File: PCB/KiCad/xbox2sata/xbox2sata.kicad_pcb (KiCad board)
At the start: 4 copper layers, 156 x 90 mm, 7 parts, among them J1 61203921621, J2 67800-8025, J3 90151-2140, U1 88SA8052, Y1 ABLS-25.000MHZ-B4-F-T

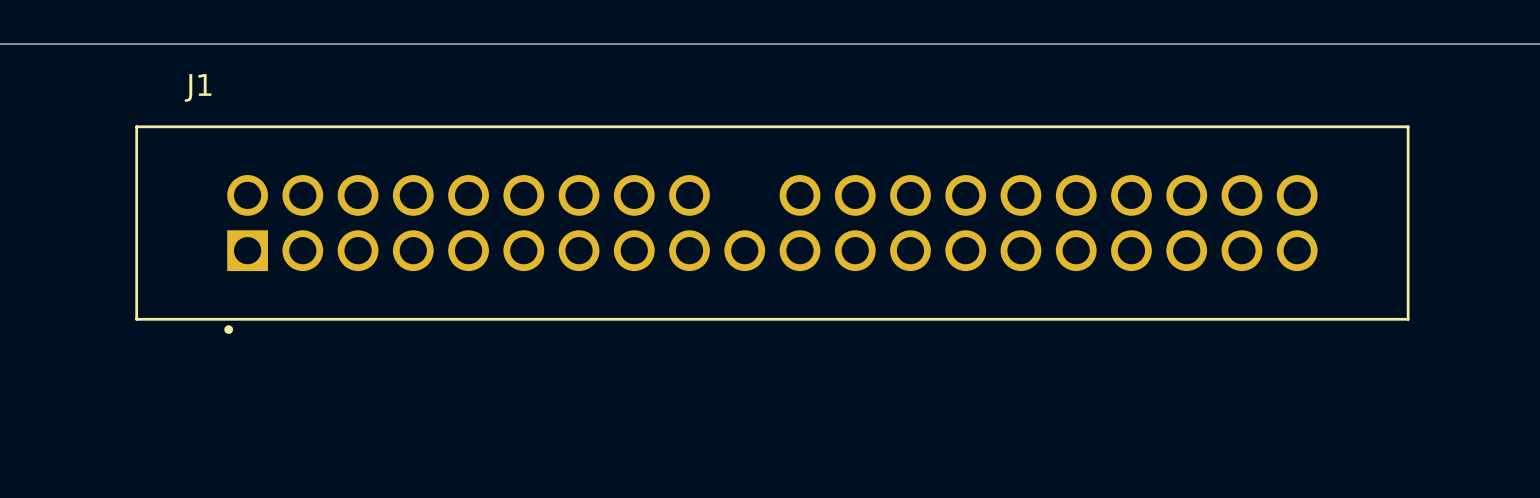
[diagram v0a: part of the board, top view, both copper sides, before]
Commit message: PCB folder structure
Created two sub folders in PCB; Proteus and KiCad and moved respective files into folders.
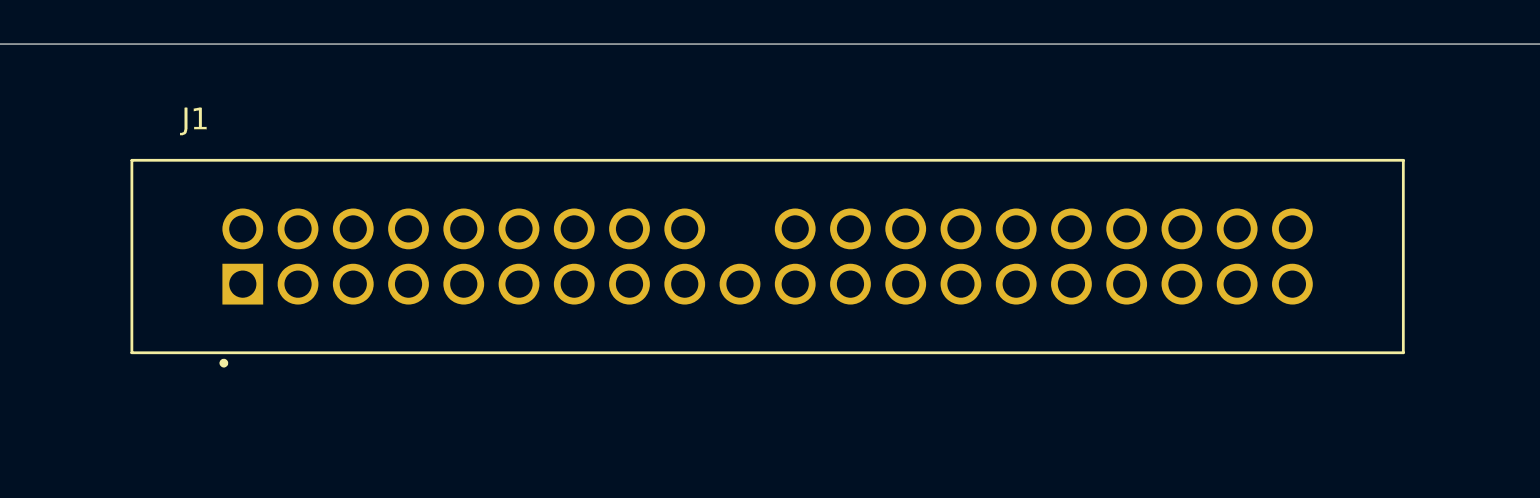
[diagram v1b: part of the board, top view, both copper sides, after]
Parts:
- moved J1 1.56 mm to (167.7, 73.3)
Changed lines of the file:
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@@
 			(pintype "power_in")
 		)
-		(model "${KICAD8_3DMODEL_DIR}/Package_DFN_QFN.3dshapes/QFN-64-1EP_9x9mm_P0.5mm_EP3.4x3.4mm.wrl"
+		(model "${KICAD8_3DMODEL_DIR}/Package_DFN_QFN.3dshapes/QFN-64-1EP_9x9mm_P0.5mm_EP7.35x7.35mm.step"
 			(offset
 				(xyz 0 0 0)
@@
 			(pintype "passive")
 		)
-		(model "D:/Gaming hardware/Microsoft XBox/Modifications/HDD/XBox-IDE to-SATA/PCB/Imports/LIB_ABLS-25.000MHZ-B4-F-T KiCad/ABLS-25.000MHZ-B4-F-T.stp"
+		(model "D:/Gaming hardware/Microsoft XBox/Modifications/HDD/XBox-IDE to-SATA/PCB/KiCad/Imports/LIB_ABLS-25.000MHZ-B4-F-T KiCad/ABLS-25.000MHZ-B4-F-T.stp"
 			(offset
 				(xyz 0 0 2.7)
@@
 	(footprint "xbox2sata:WURTH-ELEKTRONIK_61203921621"
 		(layer "F.Cu")
-		(at 167.87 71.73)
+		(at 167.65 73.27)
 		(descr "IDE socket")
 		(tags "IDE socket")
@@
 			)
 		)
-		(property "Description" "IDE Socket"
+		(property "Description" "IDE male header"
 			(at 8.5 6 0)
 			(unlocked yes)
@@
 			)
 		)
+		(sheetname "Root")
+		(sheetfile "xbox2sata.kicad_sch")
 		(attr through_hole)
 		(fp_line
@@
 			(solder_mask_margin 0.102)
 		)
-		(model "D:/Gaming hardware/Microsoft XBox/Modifications/HDD/XBox-IDE to-SATA/PCB/Imports/1761633-2.stp"
+		(model "D:/Gaming hardware/Microsoft XBox/Modifications/HDD/XBox-IDE to-SATA/PCB/KiCad/Imports/61203921621_Download_STP_61203921621_rev1.stp"
 			(offset
-				(xyz 0 0 9.5)
+				(xyz 0 0 5)
 			)
 			(scale
@@
 			(pintype "power_in")
 		)
-		(model "D:/Gaming hardware/Microsoft XBox/Modifications/HDD/XBox-IDE to-SATA/PCB/Imports/678008025.stp"
+		(model "D:/Gaming hardware/Microsoft XBox/Modifications/HDD/XBox-IDE to-SATA/PCB/KiCad/Imports/678008025.stp"
 			(offset
 				(xyz -4 0.8 4)
@@
 			(pintype "passive")
 		)
-		(model "D:/Gaming hardware/Microsoft XBox/Modifications/HDD/XBox-IDE to-SATA/PCB/Imports/Molex 90151-2140 KiCad/90151-2140.stp"
+		(model "D:/Gaming hardware/Microsoft XBox/Modifications/HDD/XBox-IDE to-SATA/PCB/KiCad/Imports/Molex 90151-2140 KiCad/90151-2140.stp"
 			(offset
 				(xyz 24.1 1.3 4)

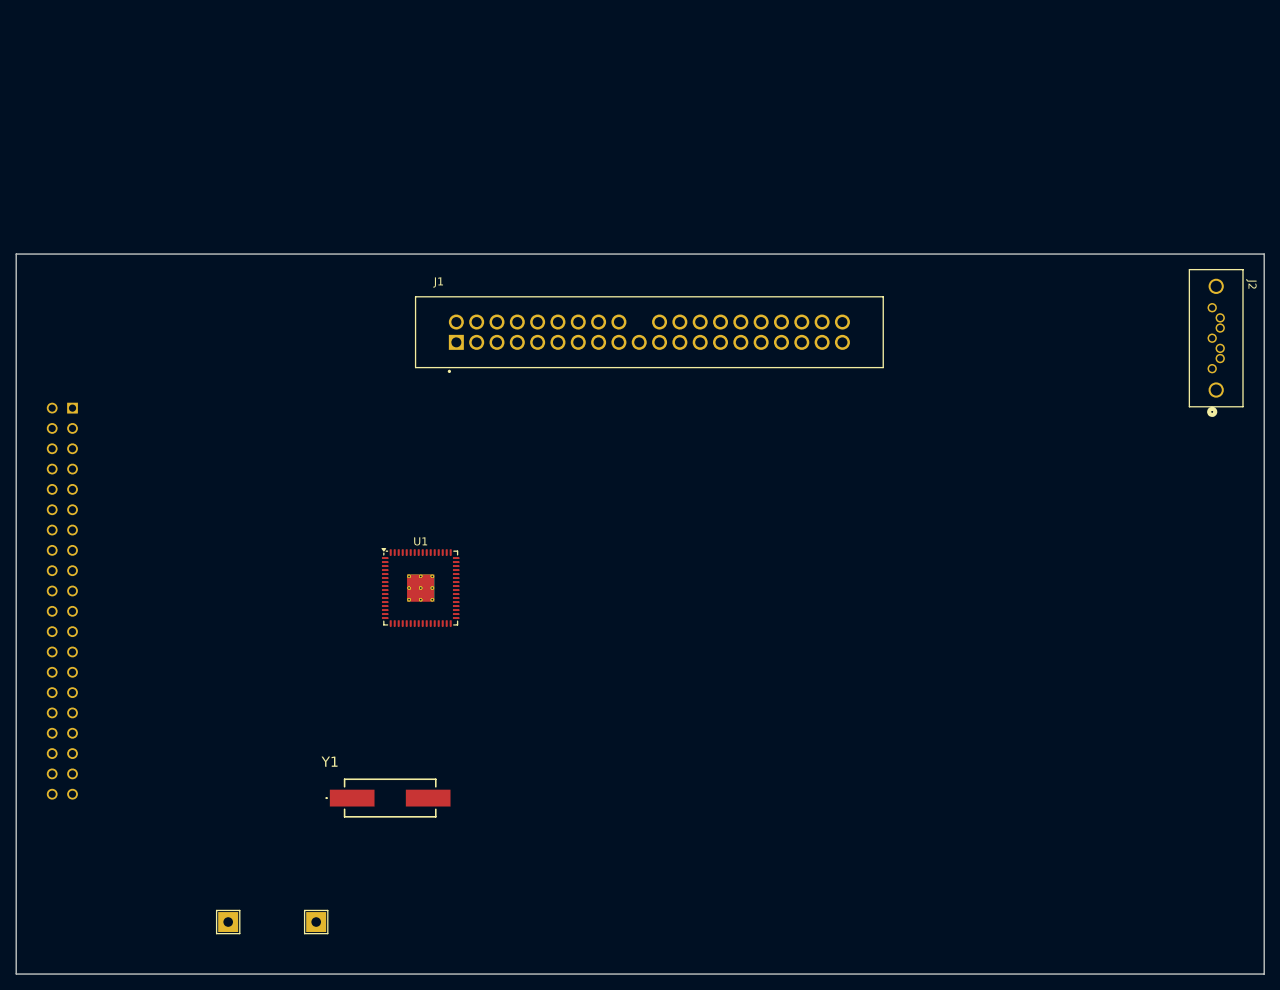
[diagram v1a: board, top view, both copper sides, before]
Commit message: KiCad updates
Nets and some components added
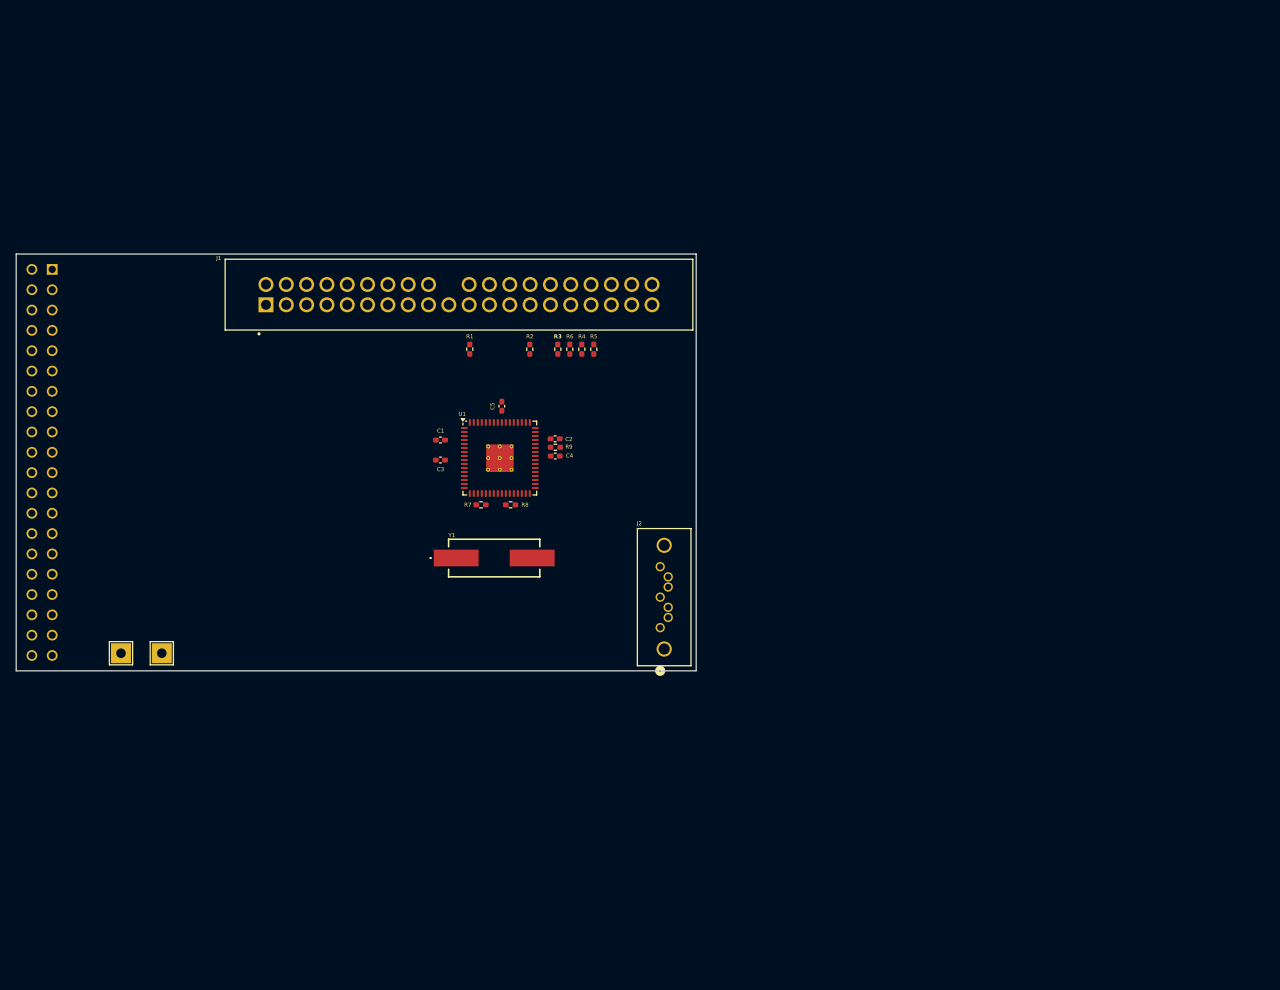
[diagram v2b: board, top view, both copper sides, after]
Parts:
- added C1: 100nF, Capacitor_SMD:C_0402_1005Metric_Pad0.74x0.62mm_HandSolder, F.Cu at (141.5, 86.8)
- added C2: 100nF, Capacitor_SMD:C_0402_1005Metric_Pad0.74x0.62mm_HandSolder, F.Cu at (155.9, 86.6)
- added C3: 100nF, Capacitor_SMD:C_0402_1005Metric_Pad0.74x0.62mm_HandSolder, F.Cu at (141.5, 89.2)
- added C4: 100nF, Capacitor_SMD:C_0402_1005Metric_Pad0.74x0.62mm_HandSolder, F.Cu at (155.9, 88.8)
- added C5: 100nF, Capacitor_SMD:C_0402_1005Metric_Pad0.74x0.62mm_HandSolder, F.Cu at (149.2, 82.5)
- added R1: 5.6K, Resistor_SMD:R_0402_1005Metric_Pad0.72x0.64mm_HandSolder, F.Cu at (145.2, 75.4)
- added R2: 4.7K, Resistor_SMD:R_0402_1005Metric_Pad0.72x0.64mm_HandSolder, F.Cu at (152.7, 75.4)
- added R3: 10K, Resistor_SMD:R_0402_1005Metric_Pad0.72x0.64mm_HandSolder, F.Cu at (156.2, 75.4)
- added R4: 10K, Resistor_SMD:R_0402_1005Metric_Pad0.72x0.64mm_HandSolder, F.Cu at (159.2, 75.4)
- added R5: 10K, Resistor_SMD:R_0402_1005Metric_Pad0.72x0.64mm_HandSolder, F.Cu at (160.7, 75.4)
- added R6: 10K, Resistor_SMD:R_0402_1005Metric_Pad0.72x0.64mm_HandSolder, F.Cu at (157.7, 75.4)
- added R7: 10K, Resistor_SMD:R_0402_1005Metric_Pad0.72x0.64mm_HandSolder, F.Cu at (146.6, 94.8)
- added R8: 10K, Resistor_SMD:R_0402_1005Metric_Pad0.72x0.64mm_HandSolder, F.Cu at (150.3, 94.8)
- added R9: 10K, Resistor_SMD:R_0402_1005Metric_Pad0.72x0.64mm_HandSolder, F.Cu at (155.9, 87.7)
- moved J2 76.2 mm to (169.0, 110.2)
- moved TP1 41.5 mm to (101.6, 113.4)
- moved TP2 34.6 mm to (106.7, 113.4)
- moved Y1 32.7 mm to (148.2, 101.5)
- moved J1 24.3 mm to (143.8, 68.6)
- moved U1 19.0 mm to (148.9, 89.0)
- moved J3 17.5 mm to (93.0, 65.4)
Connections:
- J1 pad 1: unconnected-(J1-Pad1) -> RESET-
- J1 pad 10: unconnected-(J1-Pad10) -> DD11
- J1 pad 11: unconnected-(J1-Pad11) -> DD3
- J1 pad 12: unconnected-(J1-Pad12) -> DD12
- J1 pad 13: unconnected-(J1-Pad13) -> DD2
- J1 pad 14: unconnected-(J1-Pad14) -> DD13
- J1 pad 15: unconnected-(J1-Pad15) -> DD1
- J1 pad 16: unconnected-(J1-Pad16) -> DD14
- J1 pad 17: unconnected-(J1-Pad17) -> DD0
- J1 pad 18: unconnected-(J1-Pad18) -> DD15
- J1 pad 19: unconnected-(J1-Pad19) -> GND
- J1 pad 2: unconnected-(J1-Pad2) -> GND
- J1 pad 21: unconnected-(J1-Pad21) -> DMARQ
- J1 pad 22: unconnected-(J1-Pad22) -> GND
- J1 pad 23: unconnected-(J1-Pad23) -> DIOW-
- J1 pad 24: unconnected-(J1-Pad24) -> GND
- J1 pad 25: unconnected-(J1-Pad25) -> DIOR-
- J1 pad 26: unconnected-(J1-Pad26) -> GND
- J1 pad 27: unconnected-(J1-Pad27) -> IORDY
- J1 pad 28: unconnected-(J1-Pad28) -> CSEL
- J1 pad 29: unconnected-(J1-Pad29) -> DMACK-
- J1 pad 3: unconnected-(J1-Pad3) -> DD7
- J1 pad 30: unconnected-(J1-Pad30) -> GND
- J1 pad 31: unconnected-(J1-Pad31) -> INTRQ
- J1 pad 32: unconnected-(J1-Pad32) -> Net-(J1-Pad32)
- J1 pad 33: unconnected-(J1-Pad33) -> DA1
- J1 pad 34: unconnected-(J1-Pad34) -> PDIAG-
- J1 pad 35: unconnected-(J1-Pad35) -> DA0
- J1 pad 36: unconnected-(J1-Pad36) -> DA2
- J1 pad 37: unconnected-(J1-Pad37) -> CS0-
- J1 pad 38: unconnected-(J1-Pad38) -> CS1-
- J1 pad 39: unconnected-(J1-Pad39) -> Net-(J1-Pad39)
- J1 pad 4: unconnected-(J1-Pad4) -> DD8
- J1 pad 40: unconnected-(J1-Pad40) -> GND
- J1 pad 5: unconnected-(J1-Pad5) -> DD6
- J1 pad 6: unconnected-(J1-Pad6) -> DD9
- J1 pad 7: unconnected-(J1-Pad7) -> DD5
- J1 pad 8: unconnected-(J1-Pad8) -> DD10
- J1 pad 9: unconnected-(J1-Pad9) -> DD4
- J3 pad 1: unconnected-(J3-Pad1) -> RESET-
- J3 pad 10: unconnected-(J3-Pad10) -> DD11
- J3 pad 11: unconnected-(J3-Pad11) -> DD3
- J3 pad 12: unconnected-(J3-Pad12) -> DD12
- J3 pad 13: unconnected-(J3-Pad13) -> DD2
- J3 pad 14: unconnected-(J3-Pad14) -> DD13
- J3 pad 15: unconnected-(J3-Pad15) -> DD1
- J3 pad 16: unconnected-(J3-Pad16) -> DD14
- J3 pad 17: unconnected-(J3-Pad17) -> DD0
- J3 pad 18: unconnected-(J3-Pad18) -> DD15
- J3 pad 19: unconnected-(J3-Pad19) -> GND
- J3 pad 2: unconnected-(J3-Pad2) -> GND
- J3 pad 21: unconnected-(J3-Pad21) -> DMARQ
- J3 pad 22: unconnected-(J3-Pad22) -> GND
- J3 pad 23: unconnected-(J3-Pad23) -> DIOW-
- J3 pad 24: unconnected-(J3-Pad24) -> GND
- J3 pad 25: unconnected-(J3-Pad25) -> DIOR-
- J3 pad 26: unconnected-(J3-Pad26) -> GND
- J3 pad 27: unconnected-(J3-Pad27) -> IORDY
- J3 pad 28: unconnected-(J3-Pad28) -> CSEL
- J3 pad 29: unconnected-(J3-Pad29) -> DMACK-
- J3 pad 3: unconnected-(J3-Pad3) -> DD7
- J3 pad 30: unconnected-(J3-Pad30) -> GND
- J3 pad 31: unconnected-(J3-Pad31) -> INTRQ
- J3 pad 32: unconnected-(J3-Pad32) -> IOCS16
- J3 pad 33: unconnected-(J3-Pad33) -> DA1
- J3 pad 34: unconnected-(J3-Pad34) -> PDIAG-
- J3 pad 35: unconnected-(J3-Pad35) -> DA0
- J3 pad 36: unconnected-(J3-Pad36) -> DA2
- J3 pad 37: unconnected-(J3-Pad37) -> CS0-
- J3 pad 38: unconnected-(J3-Pad38) -> CS1-
- J3 pad 39: unconnected-(J3-Pad39) -> DASP-
- J3 pad 4: unconnected-(J3-Pad4) -> DD8
- J3 pad 40: unconnected-(J3-Pad40) -> GND
- J3 pad 5: unconnected-(J3-Pad5) -> DD6
- J3 pad 6: unconnected-(J3-Pad6) -> DD9
- J3 pad 7: unconnected-(J3-Pad7) -> DD5
- J3 pad 8: unconnected-(J3-Pad8) -> DD10
- J3 pad 9: unconnected-(J3-Pad9) -> DD4
- TP1 pad 1: unconnected-(TP1-Pad1) -> GND
- TP2 pad 1: unconnected-(TP2-Pad1) -> 3V3
- U1 pad 1: unconnected-(U1-H_DD13-Pad1) -> DD13
- U1 pad 10: unconnected-(U1-H_DD10-Pad10) -> DD10
- U1 pad 11: unconnected-(U1-H_DD5-Pad11) -> DD5
- U1 pad 12: unconnected-(U1-H_DD9-Pad12) -> DD9
- U1 pad 13: unconnected-(U1-H_DD6-Pad13) -> DD6
- U1 pad 14: unconnected-(U1-H_DD8-Pad14) -> DD8
- U1 pad 15: unconnected-(U1-H_DD7-Pad15) -> DD7
- U1 pad 16: unconnected-(U1-H_RESET_N-Pad16) -> RESET-
- U1 pad 17: unconnected-(U1-RST_N-Pad17) -> RST-
- U1 pad 18: unconnected-(U1-CNFG0-Pad18) -> CNFG0
- U1 pad 19: unconnected-(U1-CNFG1-Pad19) -> CNFG1
- U1 pad 2: unconnected-(U1-H_DD2-Pad2) -> DD2
- U1 pad 20: unconnected-(U1-CNFG2-Pad20) -> CNFG2
- U1 pad 21: unconnected-(U1-ATAIOS-Pad21) -> Net-(U1-ATAIOS)
- U1 pad 22: unconnected-(U1-XTLIN/OSC-Pad22) -> XTLIN
- U1 pad 23: unconnected-(U1-XTLOUT-Pad23) -> XTLOUT
- U1 pad 24: unconnected-(U1-VAA-Pad24) -> VAA
- U1 pad 25: unconnected-(U1-VSS-Pad25) -> VSS
- U1 pad 26: unconnected-(U1-ISET-Pad26) -> Net-(U1-ISET)
- U1 pad 27: unconnected-(U1-RX_P-Pad27) -> RX_P
- U1 pad 28: unconnected-(U1-RX_M-Pad28) -> RX_M
- U1 pad 29: unconnected-(U1-VAA-Pad29) -> VAA
- U1 pad 3: unconnected-(U1-H_DD12-Pad3) -> DD12
- U1 pad 30: unconnected-(U1-VSS-Pad30) -> VSS
- U1 pad 31: unconnected-(U1-TX_M-Pad31) -> TX_M
- U1 pad 32: unconnected-(U1-TX_P-Pad32) -> TX_P
- U1 pad 33: unconnected-(U1-T0-Pad33) -> T0
- U1 pad 34: unconnected-(U1-T1-Pad34) -> PDIAG
- U1 pad 35: unconnected-(U1-T2-Pad35) -> T1
- U1 pad 36: unconnected-(U1-T3-Pad36) -> T3
- U1 pad 37: unconnected-(U1-T4-Pad37) -> T4
- U1 pad 38: unconnected-(U1-T5-Pad38) -> T5
- U1 pad 39: unconnected-(U1-T6-Pad39) -> T6
- U1 pad 4: unconnected-(U1-VDDIO-Pad4) -> 3V3
- U1 pad 40: unconnected-(U1-T7-Pad40) -> T7
- U1 pad 41: unconnected-(U1-VDD-Pad41) -> 1V2
- U1 pad 42: unconnected-(U1-GND-Pad42) -> GND
- U1 pad 43: unconnected-(U1-UAI-Pad43) -> Net-(U1-UAI)
- U1 pad 44: unconnected-(U1-VDDIO-Pad44) -> 3V3
- U1 pad 45: unconnected-(U1-UAO-Pad45) -> LED-
- U1 pad 46: unconnected-(U1-H_PDIAG_N-Pad46) -> PDIAG-
- U1 pad 47: unconnected-(U1-H_CS_N1-Pad47) -> CS1-
- U1 pad 48: unconnected-(U1-H_CS_N0-Pad48) -> CS0-
- U1 pad 49: unconnected-(U1-H_DA2-Pad49) -> DA2
- U1 pad 5: unconnected-(U1-H_DD3-Pad5) -> DD3
- U1 pad 50: unconnected-(U1-H_DA0-Pad50) -> DA0
- U1 pad 51: unconnected-(U1-H_DA1-Pad51) -> DA1
- U1 pad 52: unconnected-(U1-T8-Pad52) -> T8
- U1 pad 53: unconnected-(U1-H_INTRQ-Pad53) -> INTRQ
- U1 pad 54: unconnected-(U1-H_DMACK_N-Pad54) -> DMACK-
- U1 pad 55: unconnected-(U1-H_IORDY-Pad55) -> IORDY
- U1 pad 56: unconnected-(U1-VDD-Pad56) -> 1V2
- U1 pad 57: unconnected-(U1-GND-Pad57) -> GND
- U1 pad 58: unconnected-(U1-H_DIOR_N-Pad58) -> DIOR-
- U1 pad 59: unconnected-(U1-H_DIOW_N-Pad59) -> DIOW-
- U1 pad 6: unconnected-(U1-H_DD11-Pad6) -> DD11
- U1 pad 60: unconnected-(U1-H_DMARQ-Pad60) -> DMARQ
- U1 pad 61: unconnected-(U1-H_DD15-Pad61) -> DD15
- U1 pad 62: unconnected-(U1-H_DD0-Pad62) -> DD0
- U1 pad 63: unconnected-(U1-H_DD14-Pad63) -> DD14
- U1 pad 64: unconnected-(U1-H_DD1-Pad64) -> DD1
- U1 pad 7: unconnected-(U1-H_DD4-Pad7) -> DD4
- U1 pad 8: unconnected-(U1-GND-Pad8) -> GND
- U1 pad 9: unconnected-(U1-VDD-Pad9) -> 1V2
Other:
- board size 156 x 90 mm -> 85 x 52.1 mm

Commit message: KiCad update
Added to schematic and pcb
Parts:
- added C10: 10nF, Resistor_SMD:R_0402_1005Metric_Pad0.72x0.64mm_HandSolder, F.Cu at (123.4, 74.5)
- added C11: 10nF, Resistor_SMD:R_0402_1005Metric_Pad0.72x0.64mm_HandSolder, F.Cu at (123.4, 73.3)
- added C12: 10nF, Resistor_SMD:R_0402_1005Metric_Pad0.72x0.64mm_HandSolder, F.Cu at (123.2, 66.6)
- added C13: 10nF, Resistor_SMD:R_0402_1005Metric_Pad0.72x0.64mm_HandSolder, F.Cu at (123.3, 65.1)
- added C14: 10nF, Capacitor_SMD:C_0402_1005Metric_Pad0.74x0.62mm_HandSolder, F.Cu at (118.9, 111.4)
- added C15: 100nF, Capacitor_SMD:C_0402_1005Metric_Pad0.74x0.62mm_HandSolder, F.Cu at (118.9, 108.9)
- added C16: 100nF, Capacitor_SMD:C_0402_1005Metric_Pad0.74x0.62mm_HandSolder, F.Cu at (118.9, 107.7)
- added C17: 10nF, Capacitor_SMD:C_0402_1005Metric_Pad0.74x0.62mm_HandSolder, F.Cu at (118.9, 106.4)
- added C6: 1uF, Capacitor_SMD:C_0603_1608Metric_Pad1.08x0.95mm_HandSolder, F.Cu at (113.9, 103.2)
- added C7: 1uF, Capacitor_SMD:C_0603_1608Metric_Pad1.08x0.95mm_HandSolder, F.Cu at (114.4, 113.7)
- added C8: 18pF, Capacitor_SMD:C_0402_1005Metric_Pad0.74x0.62mm_HandSolder, F.Cu at (108.9, 81.1)
- added C9: 18pF, Capacitor_SMD:C_0402_1005Metric_Pad0.74x0.62mm_HandSolder, F.Cu at (118.5, 81.1)
- added IC1: TLV1117LV12DCYR, xbox2sata:SOT230P700X180-4N, F.Cu at (113.0, 108.4)
- added L1: L, Inductor_SMD:L_0402_1005Metric_Pad0.77x0.64mm_HandSolder, F.Cu at (118.9, 110.2)
- added R10: 1M, Resistor_SMD:R_0402_1005Metric_Pad0.72x0.64mm_HandSolder, F.Cu at (113.2, 90.0)
- added R11: 100, Resistor_SMD:R_0402_1005Metric_Pad0.72x0.64mm_HandSolder, F.Cu at (107.7, 69.9)
- added R12: 10K, Resistor_SMD:R_0402_1005Metric_Pad0.72x0.64mm_HandSolder, F.Cu at (107.8, 63.5)
- added R13: 10K, Resistor_SMD:R_0402_1005Metric_Pad0.72x0.64mm_HandSolder, F.Cu at (107.6, 65.0)
- added R14: 10K, Resistor_SMD:R_0402_1005Metric_Pad0.72x0.64mm_HandSolder, F.Cu at (107.7, 66.8)
- added R15: 4.7K, Resistor_SMD:R_0402_1005Metric_Pad0.72x0.64mm_HandSolder, F.Cu at (110.4, 76.3)
- added R16: 10K, Resistor_SMD:R_0402_1005Metric_Pad0.72x0.64mm_HandSolder, F.Cu at (112.5, 76.4)
- added R17: 10K, Resistor_SMD:R_0402_1005Metric_Pad0.72x0.64mm_HandSolder, F.Cu at (113.7, 76.4)
- added R18: 10K, Resistor_SMD:R_0402_1005Metric_Pad0.72x0.64mm_HandSolder, F.Cu at (121.1, 71.7)
- moved R5 62.6 mm to (106.3, 106.4), turned to 180 degrees
- moved R4 60.6 mm to (106.3, 104.9), turned to 0 degrees
- moved R6 58.6 mm to (106.3, 103.4), turned to 180 degrees
- moved R3 56.5 mm to (106.3, 101.9), turned to 0 degrees
- moved J2 54.3 mm to (128.2, 74.4)
- moved R2 51.8 mm to (106.3, 98.4), turned to 0 degrees
- moved J1 49.0 mm to (99.6, 89.6), turned to -90 degrees
- moved R8 48.5 mm to (107.7, 71.6), turned to 0 degrees
- moved R7 47.0 mm to (107.8, 68.3)
- moved C4 42.8 mm to (114.9, 76.4), turned to -90 degrees
- moved R1 41.9 mm to (106.3, 90.9), turned to 0 degrees
- moved R9 41.5 mm to (116.0, 76.4), turned to -90 degrees
- moved C2 40.2 mm to (117.0, 76.4), turned to -90 degrees
- moved U1 39.5 mm to (114.6, 69.5), turned to -90 degrees
- moved C3 38.4 mm to (114.4, 62.1), turned to 90 degrees
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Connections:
- J2 pad 1: unconnected-(J2-Pad1) -> GND
- J2 pad 2: unconnected-(J2-Pad2) -> Net-(C10-Pad2)
- J2 pad 3: unconnected-(J2-Pad3) -> Net-(C11-Pad2)
- J2 pad 4: unconnected-(J2-Pad4) -> GND
- J2 pad 5: unconnected-(J2-Pad5) -> Net-(C12-Pad2)
- J2 pad 6: unconnected-(J2-Pad6) -> Net-(C13-Pad2)
- J2 pad 7: unconnected-(J2-Pad7) -> GND
- J2 pad 8: unconnected-(J2-mount_1-Pad8) -> GND
- J2 pad 9: unconnected-(J2-mount_2-Pad9) -> GND
- U1 pad 37: T4 -> GND
- Y1 pad 1: unconnected-(Y1-Pad1) -> Net-(C8-Pad1)
- Y1 pad 2: unconnected-(Y1-Pad2) -> XTLIN
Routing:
- net 1V2: track 0.00 -> 12.3 mm
- net 3V3: track 0.00 -> 7.88 mm
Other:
- board size 85 x 52.1 mm -> 43.9 x 59.3 mm
- copper layers 4 -> 2
- board text added: "${REFERENCE}"
- board text added: "xbox 3V3"
- board text added: "xbox GND"
- board text added: "xbox2sata"

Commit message: slight changes to schematic
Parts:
- moved J1 53.9 mm to (135.3, 49.2), turned to 180 degrees
- moved J2 33.1 mm to (160.6, 67.3)
- moved J3 17.0 mm to (109.7, 62.3)
- moved C9 11.9 mm to (128.8, 75.2)
- moved R1 11.9 mm to (116.6, 85.0)
- moved R11 11.9 mm to (118.1, 64.0)
- moved R13 11.9 mm to (118.0, 59.1)
- moved R15 11.9 mm to (120.8, 70.4)
- moved R9 11.9 mm to (126.3, 70.5)
- moved R12 11.9 mm to (118.1, 57.6)
- moved C10 11.9 mm to (133.7, 68.6)
- moved C12 11.9 mm to (133.6, 60.7)
- moved R17 11.9 mm to (124.1, 70.5)
- moved Y1 11.9 mm to (123.9, 79.9)
- moved C1 11.9 mm to (127.2, 56.2)
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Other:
- board size 43.9 x 59.3 mm -> 62.8 x 68.6 mm
